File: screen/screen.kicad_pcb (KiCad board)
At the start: 2 copper layers, 41.9 x 30 mm, 18 parts, among them J1 Conn_01x04_Female, J2 Conn_01x12_Female, U1 SPX3819M5-L-3-3, U2 ESP-12E

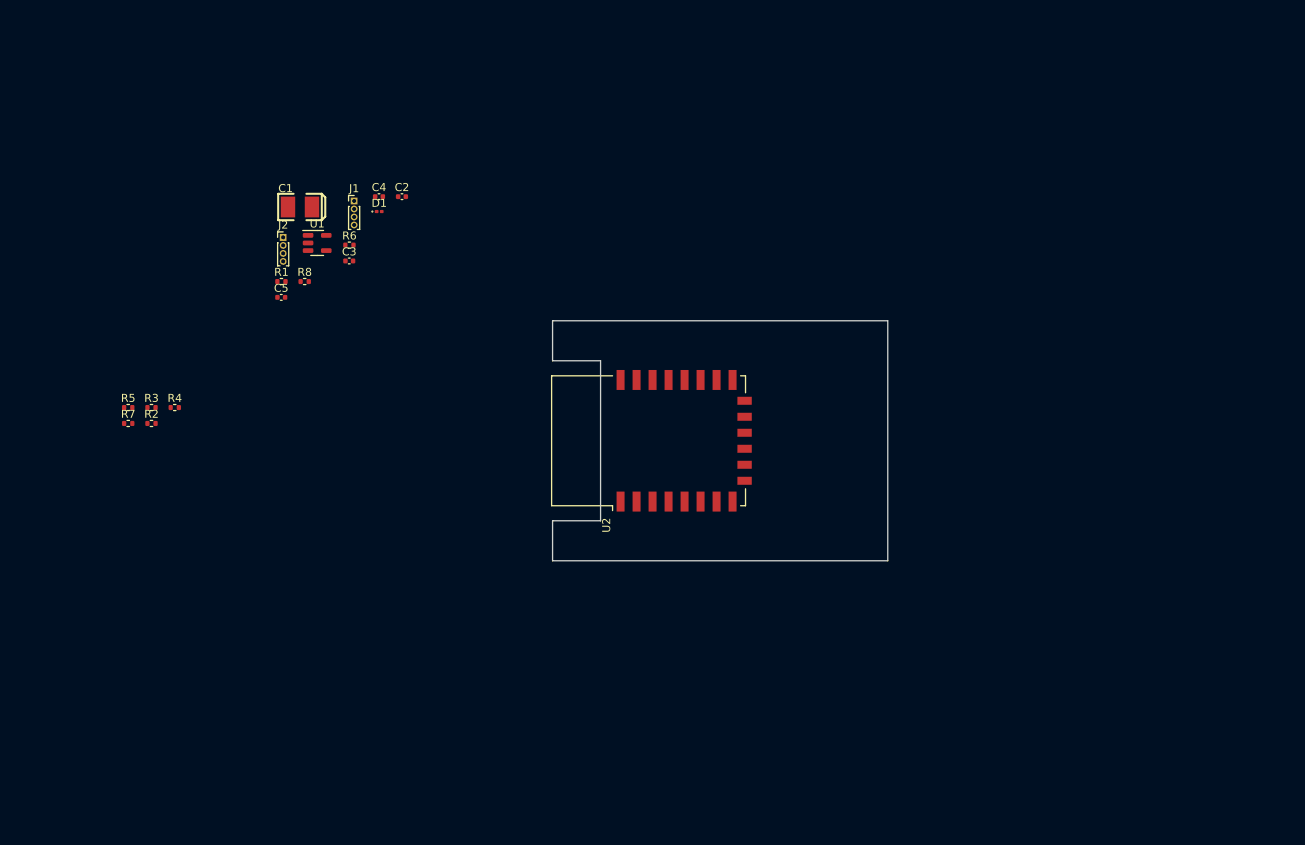
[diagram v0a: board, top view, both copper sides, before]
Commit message: add tft footprint
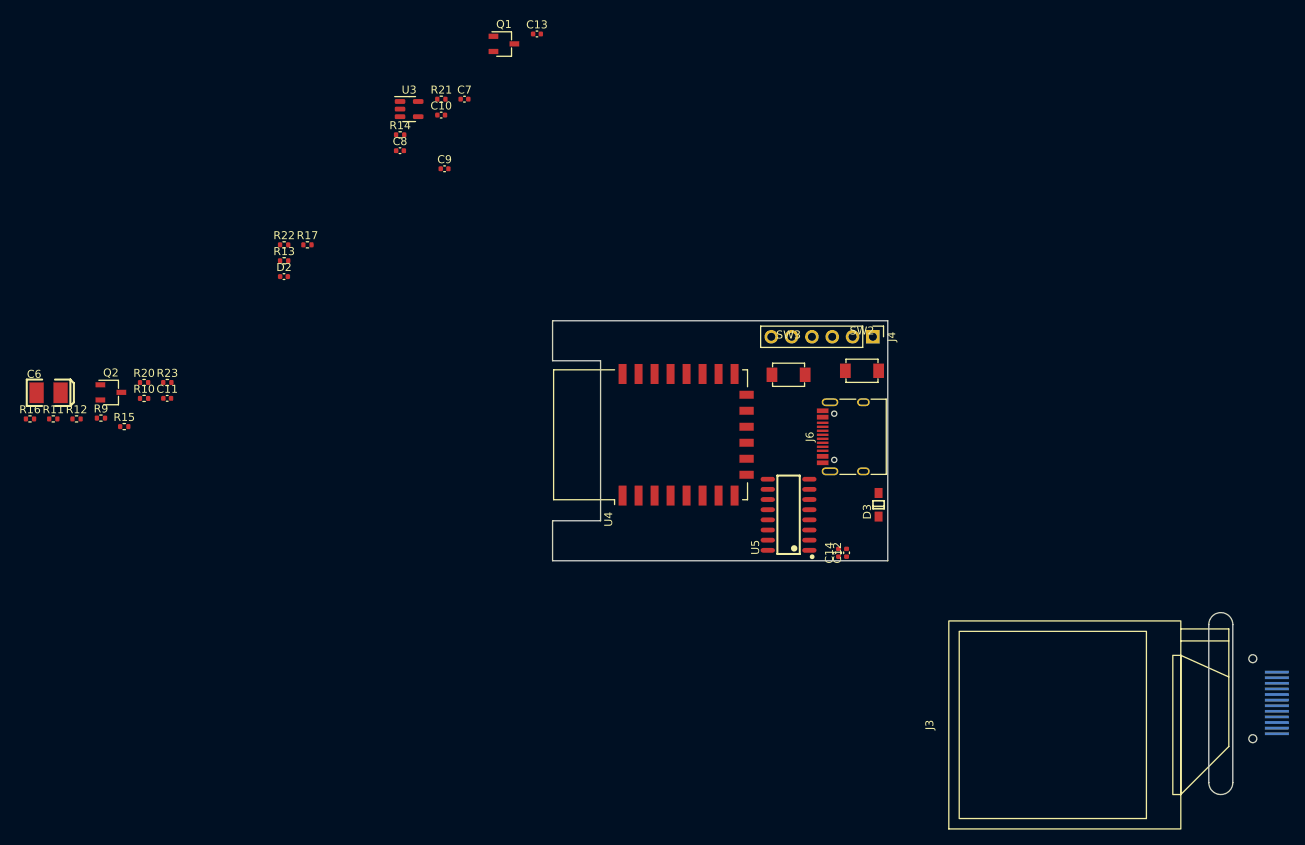
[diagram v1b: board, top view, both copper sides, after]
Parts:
- removed C1: 100uf, lc_lib:CASE-B_3528
- removed C2: 1uf, Capacitor_SMD:C_0402_1005Metric
- removed C3, C5: 470pf, Capacitor_SMD:C_0402_1005Metric
- removed C4: 10uf, Capacitor_SMD:C_0402_1005Metric
- removed D1: 3.3, LED_SMD:LED_0201_0603Metric
- removed J1: Conn_01x04_Female, Connector_PinHeader_1.00mm:PinHeader_1x04_P1.00mm_Vertical
- removed J2: Conn_01x12_Female, Connector_PinHeader_1.00mm:PinHeader_1x04_P1.00mm_Vertical
- removed R1, R3, R7, R8: 12K, Resistor_SMD:R_0402_1005Metric
- removed R2, R5: 470, Resistor_SMD:R_0402_1005Metric
- removed R4: 12k, Resistor_SMD:R_0402_1005Metric
- removed R6: 0, Resistor_SMD:R_0402_1005Metric
- removed U1: SPX3819M5-L-3-3, Package_TO_SOT_SMD:SOT-23-5
- removed U2: ESP-12E, RF_Module:ESP-12E
- added C10: 470pf, Capacitor_SMD:C_0402_1005Metric, F.Cu at (95.1, 59.3)
- added C11: 10uf, Capacitor_SMD:C_0402_1005Metric, F.Cu at (60.8, 94.7)
- added C12: 100nf, Capacitor_SMD:C_0402_1005Metric, F.Cu at (145.8, 114.0)
- added C13: 100nf, Capacitor_SMD:C_0402_1005Metric, F.Cu at (107.0, 49.1)
- added C14: 10uf, Capacitor_SMD:C_0402_1005Metric, F.Cu at (144.8, 114.0)
- added C6: 100uf, lc_lib:CASE-B_3528, F.Cu at (46.0, 94.0)
- added C7: 1uf, Capacitor_SMD:C_0402_1005Metric, F.Cu at (98.0, 57.3)
- added C8: 470pf, Capacitor_SMD:C_0402_1005Metric, F.Cu at (89.9, 63.7)
- added C9: 10uf, Capacitor_SMD:C_0402_1005Metric, F.Cu at (95.5, 66.0)
- added D2: 3.3, Capacitor_SMD:C_0402_1005Metric, F.Cu at (75.4, 79.5)
- added D3: B120-E3, lc_lib:SOD-123, F.Cu at (149.8, 108.0)
- added J3: Conn_01x12_Female, My-lib:TFT_1.4_12_back, F.Cu at (193.5, 138.2)
- added J4: Conn_01x06_Female, Connector_PinHeader_2.54mm:PinHeader_1x06_P2.54mm_Vertical, F.Cu at (149.0, 87.0)
- added J6: usbc, Connector_USB:USB_C_Receptacle_HRO_TYPE-C-31-M-12, F.Cu at (146.8, 99.5)
- added Q1: q1, Package_TO_SOT_SMD:TSOT-23, F.Cu at (102.9, 50.4)
- added Q2: q2, Package_TO_SOT_SMD:TSOT-23, F.Cu at (53.8, 93.9)
- added R10: 470, Resistor_SMD:R_0402_1005Metric, F.Cu at (57.9, 94.7)
- added R11: 12K, Resistor_SMD:R_0402_1005Metric, F.Cu at (46.6, 97.3)
- added R12: 12k, Resistor_SMD:R_0402_1005Metric, F.Cu at (49.5, 97.3)
- added R13: 0, Resistor_SMD:R_0402_1005Metric, F.Cu at (75.4, 77.5)
- added R14: 470, Resistor_SMD:R_0402_1005Metric, F.Cu at (89.9, 61.8)
- added R15: 470, Resistor_SMD:R_0402_1005Metric, F.Cu at (55.5, 98.2)
- added R16: 12K, Resistor_SMD:R_0402_1005Metric, F.Cu at (43.7, 97.3)
- added R17: 12K, Resistor_SMD:R_0402_1005Metric, F.Cu at (78.4, 75.5)
- added R20: 470, Resistor_SMD:R_0402_1005Metric, F.Cu at (57.9, 92.7)
- added R21: 470, Resistor_SMD:R_0402_1005Metric, F.Cu at (95.1, 57.3)
- added R22: 12K, Resistor_SMD:R_0402_1005Metric, F.Cu at (75.4, 75.5)
- added R23: 12K, Resistor_SMD:R_0402_1005Metric, F.Cu at (60.8, 92.7)
- added R9: 12K, Resistor_SMD:R_0402_1005Metric, F.Cu at (52.5, 97.2)
- added SW2: SW_Push, My-lib:SMD,3x4x2mm, F.Cu at (147.7, 91.2)
- added SW3: SW_Push, My-lib:SMD,3x4x2mm, F.Cu at (138.5, 91.8)
- added U3: SPX3819M5-L-3-3, Package_TO_SOT_SMD:SOT-23-5, F.Cu at (91.1, 58.5)
- added U4: ESP-12E, RF_Module:ESP-12E, F.Cu at (121.2, 99.2)
- added U5: CH340C, lc_lib:SOP-16_150MIL, F.Cu at (138.5, 109.2)

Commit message: update
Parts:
- removed C11, C14: 10uf, Capacitor_SMD:C_0402_1005Metric
- removed C12, C13: 100nf, Capacitor_SMD:C_0402_1005Metric
- removed J6: usbc, Connector_USB:USB_C_Receptacle_HRO_TYPE-C-31-M-12
- removed Q1: q1, Package_TO_SOT_SMD:TSOT-23
- removed Q2: q2, Package_TO_SOT_SMD:TSOT-23
- removed R20, R21: 470, Resistor_SMD:R_0402_1005Metric
- removed R22, R23: 12K, Resistor_SMD:R_0402_1005Metric
- removed U5: CH340C, lc_lib:SOP-16_150MIL
- added C1: 10uf, Capacitor_SMD:C_0402_1005Metric, F.Cu at (136.3, 91.2)
- added C2: 10uf, Capacitor_SMD:C_0402_1005Metric, F.Cu at (137.8, 89.7)
- added D1: led-red, LED_SMD:LED_0402_1005Metric, F.Cu at (136.3, 94.3)
- added J1: USB_C_Receptacle_USB2.0, Connector_USB:USB_C_Receptacle_HRO_TYPE-C-31-M-12, F.Cu at (139.7, 106.1)
- added J2: Conn_01x02_Female, Connector_PinHeader_2.54mm:PinHeader_1x02_P2.54mm_Vertical, F.Cu at (148.8, 112.7)
- added R1: 1k, Resistor_SMD:R_0402_1005Metric, F.Cu at (136.3, 97.5)
- added R2: 1k, Resistor_SMD:R_0402_1005Metric, F.Cu at (136.3, 99.0)
- added R3: 1.2K, Resistor_SMD:R_0402_1005Metric, F.Cu at (136.3, 95.9)
- added R4: 10k, Resistor_SMD:R_0402_1005Metric, F.Cu at (120.7, 109.9)
- added R5: 10k, Resistor_SMD:R_0402_1005Metric, F.Cu at (119.8, 109.9)
- added SW1: SW_DPDT_x2, Button_Switch_SMD:SW_SPDT_PCM12, F.Cu at (147.1, 98.4)
- added U1: TP4056_[C16581], lc_lib:SOP-8_EP_150MIL, F.Cu at (141.6, 93.5)
- D2: value 3.3 -> led-white; footprint Capacitor_SMD:C_0402_1005Metric -> LED_SMD:LED_0402_1005Metric
- D3: value B120-E3 -> led-green; footprint lc_lib:SOD-123 -> LED_SMD:LED_0402_1005Metric
- J3: footprint My-lib:TFT_1.4_12_back -> My-lib:TFT_1.4_12_front; moved to B.Cu
- J4: footprint Connector_PinHeader_2.54mm:PinHeader_1x06_P2.54mm_Vertical -> Connector_PinHeader_1.27mm:PinHeader_1x06_P1.27mm_Vertical
- SW2, SW3: footprint My-lib:SMD,3x4x2mm -> My-lib:Button_SMD,3x4x2mm
- moved C6 85.0 mm to (129.3, 110.7)
- moved R11 82.3 mm to (128.5, 89.8), turned to 180 degrees
- moved J3 81.3 mm to (122.0, 99.7), turned to 180 degrees
- moved R16 75.1 mm to (117.7, 109.9), turned to -90 degrees
- moved R9 74.2 mm to (126.4, 89.8)
- moved U3 74.1 mm to (147.7, 106.3), turned to 180 degrees
- moved R12 73.2 mm to (121.6, 109.9), turned to -90 degrees
- moved R15 69.5 mm to (124.4, 89.8), turned to 180 degrees
- moved C7 69.2 mm to (149.3, 103.7)
- moved C8 69.1 mm to (146.3, 103.7), turned to 180 degrees
- moved C9 66.9 mm to (146.2, 109.6), turned to -90 degrees
- moved R10 66.5 mm to (122.7, 109.9), turned to 90 degrees
- moved R13 59.0 mm to (124.7, 109.9), turned to -90 degrees
- moved D2 57.1 mm to (123.7, 109.9), turned to -90 degrees
- moved C10 55.9 mm to (118.8, 109.9), turned to 90 degrees
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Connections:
- C7 pad 1: +5VD -> Net-(C7-Pad1)
- D3 pad 1: +5VD -> Net-(D3-Pad1)
- D3 pad 2: /VDDUSB -> Net-(D3-Pad2)
- J4 pad 1: +5VD -> +3V3
- U3 pad 1: +5VD -> +BATT
- U3 pad 3: +5VD -> Net-(C7-Pad1)
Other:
- copper layers 2 -> 4

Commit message: screen finish
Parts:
- J1: footprint Connector_USB:USB_C_Receptacle_HRO_TYPE-C-31-M-12 -> digikey-footprints:USB-C_Female_Vert_DX07S024WJ3R400
- moved D2 23.0 mm to (146.2, 113.4), turned to 90 degrees
- moved J2 21.2 mm to (148.9, 92.8), turned to 180 degrees
- moved D3 20.9 mm to (144.9, 113.4), turned to 90 degrees
- moved SW3 14.9 mm to (139.3, 111.1), turned to 0 degrees
- moved C5 13.0 mm to (142.2, 101.9), turned to 90 degrees
- moved J1 10.6 mm to (148.9, 100.8), turned to -90 degrees
- moved C4 9.51 mm to (140.0, 101.9), turned to 90 degrees
- moved C7 9.25 mm to (141.1, 101.9), turned to 90 degrees
- moved C2 8.79 mm to (137.7, 101.9), turned to 90 degrees
- moved U3 7.68 mm to (140.1, 105.2)
- moved R9 7.55 mm to (137.7, 91.6), turned to 90 degrees
- moved R14 6.91 mm to (139.9, 91.6), turned to 90 degrees
- moved R5 6.51 mm to (138.8, 101.9), turned to 90 degrees
- moved C6 5.71 mm to (142.0, 91.6), turned to 90 degrees
- moved U2 3.90 mm to (140.1, 97.1), turned to 0 degrees
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- renumbered C10 to C1, C8 to C2, C6 to C3, C7 to C4, C2 to C5, C1 to C6, C9 to C7, D2 to D1, D3 to D2, D1 to D3, J4 to J2, J2 to J3, J3 to J4, R17 to R1, R14 to R11, R4 to R13, R1 to R14, R9 to R2, R11 to R3, R15 to R4, R3 to R5, R13 to R6, R16 to R7, R5 to R8, R2 to R9, SW3 to SW1, SW1 to SW3, U4 to U1, U1 to U2
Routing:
- net +BATT: track 0.00 -> 56.0 mm, vias 0 -> 4
- net /GPIO0: track 0.00 -> 47.1 mm, vias 0 -> 3
- net GND: track 0.00 -> 47.0 mm, vias 0 -> 15
- net /nRST: track 0.00 -> 46.7 mm, vias 0 -> 2
- net Net-(C2-Pad2): track 0.00 -> 42.2 mm
- net /RXD: track 0.00 -> 37.3 mm
- net /TXD: track 0.00 -> 37.1 mm
- net Net-(D1-Pad1): track 0.00 -> 26.0 mm, vias 0 -> 2
- net Net-(D3-Pad1): track 0.00 -> 25.9 mm, vias 0 -> 2
- net Net-(D3-Pad2): track 0.00 -> 25.6 mm, vias 0 -> 2
- net Net-(D1-Pad2): track 0.00 -> 25.0 mm, vias 0 -> 2
- net +3V3: track 0.00 -> 23.6 mm, vias 0 -> 6
- net Net-(R13-Pad2): track 0.00 -> 12.7 mm
- net /GPIO13: track 0.00 -> 11.6 mm, vias 0 -> 1
- net Net-(R15-Pad2): track 0.00 -> 10.7 mm, vias 0 -> 2
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- added copper zone on In2.Cu, net +3V3
- added copper zone on B.Cu, net GND
- added copper zone on F.Cu, net GND
- added copper zone on In1.Cu, net GND
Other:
- board text added: "+"
- board text added: "3.3"
- board text added: "BT-"
- board text added: "GND"
- board text added: "GPIO0"
- board text added: "RXD"
- board text added: "Release my personality and pursuing my dream."
- board text added: "TXD"
- board text added: "mini screen Design by stone"
- board text added: "nRST"
